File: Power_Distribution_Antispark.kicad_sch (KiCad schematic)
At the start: 90 parts, among them J1 STM Signal Conn, J5 +48V Battery Conn, J6 Motor Conn, Q1 BUK9M42-60EX, Q2 G20P06K, Q3 BUK9M42-60EX, Q4 G20P06K, U1 74LVC1G14GW_125, U2 TPP60308-ES1R-S, U3 TPP60308-ES1R-S, U4 LM331AU-S5TR, U5 TLV74033PDBVR, U6 LMR51603XDBVR, U8 INA181A3IDBVR

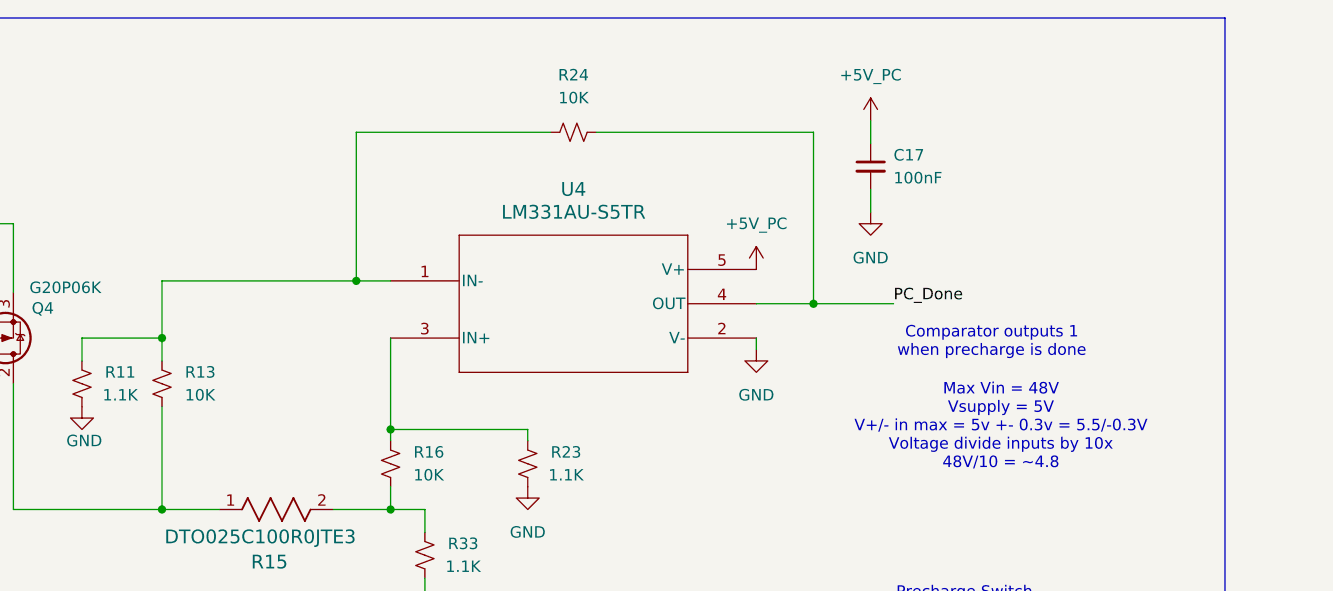
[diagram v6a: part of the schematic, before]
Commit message: added pull up resistor for comparator
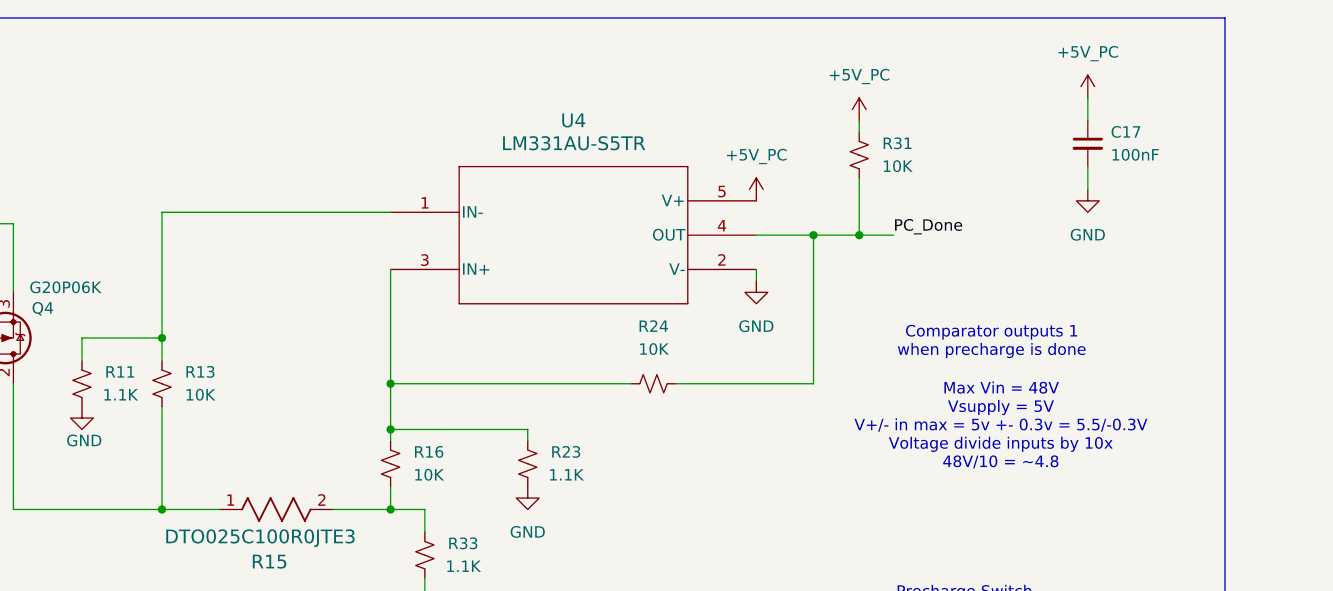
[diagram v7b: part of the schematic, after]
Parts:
- added R31: 10K, Resistor_SMD:R_0201_0603Metric, symbol Device:R_Small_US
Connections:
- net +5V_PC: now also R31.1
- net PC_Done: now also R31.2
- net at R11.2, R13.1, U4.1 (IN-): no longer R24.1
- net at R16.1, R23.2, U4.3 (IN+): now also R24.1
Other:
- moved on the sheet: C17, R24, U4

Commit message: final schematic
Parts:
- removed C21: 2.2uF, Capacitor_SMD:C_0805_2012Metric, symbol Device:C_Small
- removed C23: 100nF, Capacitor_SMD:C_0201_0603Metric, symbol Device:C_Small
- removed C25: 15uF, Capacitor_SMD:C_0201_0603Metric, symbol Device:C_Small
- removed L3: 82uH, CustomFootprintLibrary:IND_ASPI-4030S-820M-T, symbol Device:L_Small
- removed R29: 118K, Resistor_SMD:R_0201_0603Metric, symbol Device:R_Small_US
- removed R30: 22.1K, Resistor_SMD:R_0201_0603Metric, symbol Device:R_Small_US
- removed U6: LMR51603XDBVR, CustomFootprintLibrary:DBV0006A-MFG, symbol CustomLibrary:LMR51603XDBVR
- added R35, R45: 10.5K, Resistor_SMD:R_0201_0603Metric, symbol Device:R_Small_US
- added R36, R46: 1.5K, Resistor_SMD:R_0201_0603Metric, symbol Device:R_Small_US
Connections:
- net +5V_PC is gone; now on net +5V: C17.1, C24.1, C27.1, C5.1, C6.1, R31.1, U1.5 (VCC), U2.3 (EN), U3.3 (EN), U4.5 (V+), U5.3 (EN), U8.6 (V+)
- net +5V: now also R35.1, R36.1, R45.1, R46.1
- net GND: now also R36.2, R46.2
- net at C1.1, C3.1, F2.2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: now also R45.2
- net at C2.1, C4.1, F3.2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: now also R35.2
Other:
- note removed: "48V->5V Precharge Enable Control"
- moved on the sheet: C1, C11, C13, C15, C18, C2, C3, C4, C5, C7, C9, D1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
